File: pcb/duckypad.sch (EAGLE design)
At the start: 159 parts, among them IC2 REG1117, SW1 SPST_TACT-EVQQ2, SW2 SPST_TACT-EVQQ2, SW21 EC12E_SW, SW22 EC12E_SW, SW3 324_SW324_SWITCH_FOOT_HOLE, SW4 324_SW324_SWITCH_FOOT_HOLE, U1 USBC_16P, U2 USBC_16P, U3 ESP32-S3FN8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

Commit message: working on new PCB
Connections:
- removed net N$66: U3.SPICS1, X3-5.S
- net GND: now also X3-5.S
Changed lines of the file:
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@@
 <pinref part="X3" gate="-2" pin="S"/>
 <pinref part="GND64" gate="1" pin="GND"/>
-<wire x1="93.98" y1="-205.74" x2="83.82" y2="-205.74" width="0.1524" layer="91"/>
+<wire x1="93.98" y1="-205.74" x2="88.9" y2="-205.74" width="0.1524" layer="91"/>
+<pinref part="X3" gate="-5" pin="S"/>
+<wire x1="88.9" y1="-205.74" x2="83.82" y2="-205.74" width="0.1524" layer="91"/>
+<wire x1="93.98" y1="-213.36" x2="88.9" y2="-213.36" width="0.1524" layer="91"/>
+<wire x1="88.9" y1="-213.36" x2="88.9" y2="-205.74" width="0.1524" layer="91"/>
+<junction x="88.9" y="-205.74"/>
 </segment>
 <segment>
@@
 </segment>
 </net>
-<net name="N$66" class="0">
-<segment>
-<pinref part="U3" gate="G$1" pin="SPICS1"/>
-<wire x1="347.98" y1="-91.44" x2="365.76" y2="-91.44" width="0.1524" layer="91"/>
-<wire x1="365.76" y1="-91.44" x2="365.76" y2="-213.36" width="0.1524" layer="91"/>
-<wire x1="365.76" y1="-213.36" x2="93.98" y2="-213.36" width="0.1524" layer="91"/>
-<pinref part="X3" gate="-5" pin="S"/>
-</segment>
-</net>

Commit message: finishing touches
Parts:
- removed X3: SM12B-SSR-H-TB, duckypad:SM12B-SSR-H-TB
- added U$3: SH10P, duckypad:SH10P
- D1, D10, D11, D12, D13, D14, D15, D16, D17, D18, D19, D2, D20, D21, D3, D4, D5, D6, D7, D8, D9: device adafruit_changed:DIODESOD-123 -> duckypad:ADAFRUIT_CHANGED_DIODESOD-123
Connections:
- net +3V3: now also U$3.3; no longer X3-3.S
- net GND: now also U$3.11, U$3.12, U$3.2; no longer X3-12.S, X3-13.S, X3-14.S, X3-2.S, X3-5.S
- net N$1: now also U$3.1; no longer X3-1.S
- net N$37: now also U$3.4; no longer X3-4.S
- net N$67: now also U$3.5; no longer X3-6.S
- net N$68: now also U$3.6; no longer X3-7.S
- net N$69: now also U$3.7; no longer X3-8.S
- net N$70: now also U$3.8; no longer X3-9.S
- net N$72: now also U$3.9; no longer X3-10.S
- net N$73: now also U$3.10; no longer X3-11.S

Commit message: finishing touches
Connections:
- removed net N$32: C29.2, IC2.VIN, JP2.2
- new net N$66: C29.2, IC2.VIN, JP2.2, U$3.1, U1.VBUS
- net N$1: no longer U$3.1, U1.VBUS
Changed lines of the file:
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@@
 <segment>
 <pinref part="U2" gate="G$1" pin="VBUS"/>
-<wire x1="43.18" y1="-144.78" x2="78.74" y2="-144.78" width="0.1524" layer="91"/>
-<pinref part="U1" gate="G$1" pin="VBUS"/>
-<wire x1="43.18" y1="-177.8" x2="78.74" y2="-177.8" width="0.1524" layer="91"/>
-<wire x1="78.74" y1="-177.8" x2="78.74" y2="-144.78" width="0.1524" layer="91"/>
-<wire x1="78.74" y1="-144.78" x2="93.98" y2="-144.78" width="0.1524" layer="91"/>
-<junction x="78.74" y="-144.78"/>
+<wire x1="43.18" y1="-144.78" x2="93.98" y2="-144.78" width="0.1524" layer="91"/>
 <pinref part="JP2" gate="A" pin="1"/>
 <wire x1="93.98" y1="-144.78" x2="93.98" y2="-154.94" width="0.1524" layer="91"/>
-<junction x="78.74" y="-177.8"/>
-<pinref part="U$3" gate="G$1" pin="1"/>
-<wire x1="78.74" y1="-177.8" x2="124.46" y2="-177.8" width="0.1524" layer="91"/>
-<wire x1="124.46" y1="-177.8" x2="124.46" y2="-203.2" width="0.1524" layer="91"/>
 </segment>
 </net>
@@
 <pinref part="X1" gate="G$1" pin="SIGNAL"/>
 <wire x1="347.98" y1="-35.56" x2="281.94" y2="-35.56" width="0.1524" layer="91"/>
-</segment>
-</net>
-<net name="N$32" class="0">
-<segment>
-<pinref part="IC2" gate="G$1" pin="VIN"/>
-<pinref part="C29" gate="G$1" pin="2"/>
-<wire x1="119.38" y1="-144.78" x2="124.46" y2="-144.78" width="0.1524" layer="91"/>
-<wire x1="119.38" y1="-144.78" x2="96.52" y2="-144.78" width="0.1524" layer="91"/>
-<junction x="119.38" y="-144.78"/>
-<pinref part="JP2" gate="A" pin="2"/>
-<wire x1="96.52" y1="-144.78" x2="96.52" y2="-154.94" width="0.1524" layer="91"/>
 </segment>
 </net>
@@
 </segment>
 </net>
+<net name="N$66" class="0">
+<segment>
+<pinref part="U1" gate="G$1" pin="VBUS"/>
+<wire x1="43.18" y1="-177.8" x2="96.52" y2="-177.8" width="0.1524" layer="91"/>
+<pinref part="IC2" gate="G$1" pin="VIN"/>
+<pinref part="C29" gate="G$1" pin="2"/>
+<wire x1="119.38" y1="-144.78" x2="124.46" y2="-144.78" width="0.1524" layer="91"/>
+<wire x1="119.38" y1="-144.78" x2="96.52" y2="-144.78" width="0.1524" layer="91"/>
+<junction x="119.38" y="-144.78"/>
+<pinref part="JP2" gate="A" pin="2"/>
+<wire x1="96.52" y1="-144.78" x2="96.52" y2="-154.94" width="0.1524" layer="91"/>
+<pinref part="U$3" gate="G$1" pin="1"/>
+<wire x1="96.52" y1="-154.94" x2="96.52" y2="-177.8" width="0.1524" layer="91"/>
+<wire x1="96.52" y1="-177.8" x2="96.52" y2="-203.2" width="0.1524" layer="91"/>
+<wire x1="96.52" y1="-203.2" x2="124.46" y2="-203.2" width="0.1524" layer="91"/>
+<junction x="96.52" y="-154.94"/>
+<junction x="96.52" y="-177.8"/>
+</segment>
+</net>

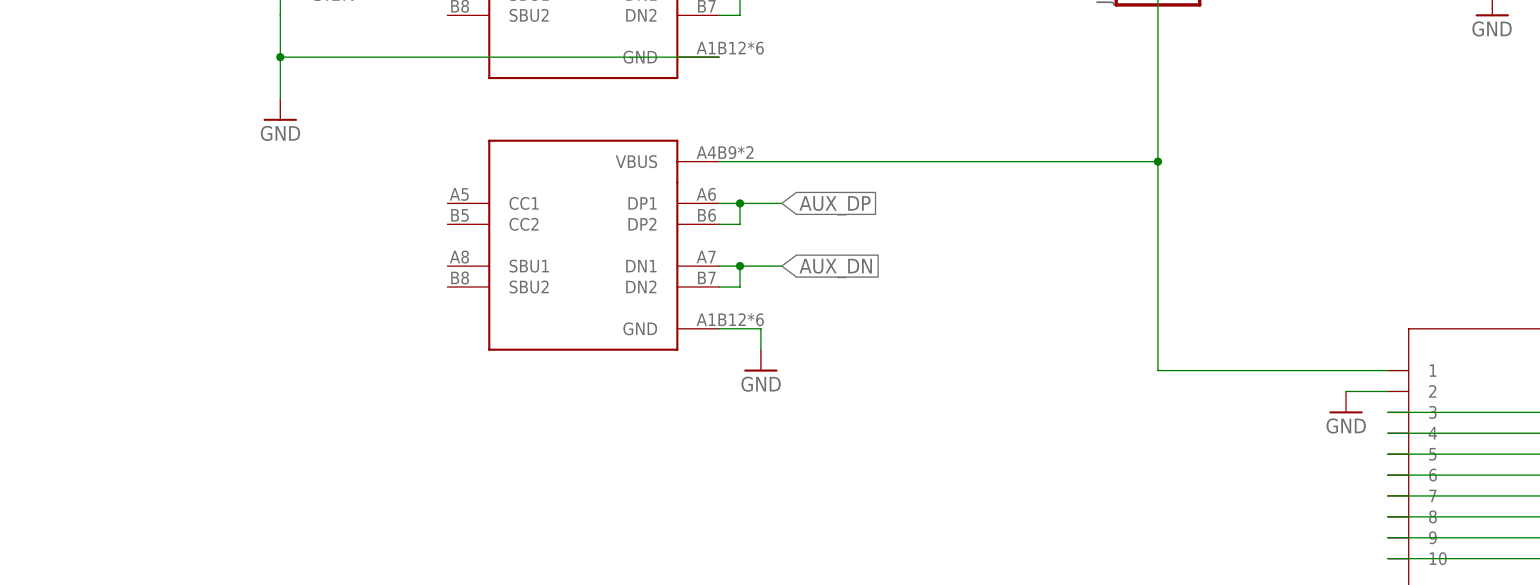
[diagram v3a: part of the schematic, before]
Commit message: wired up CC pins
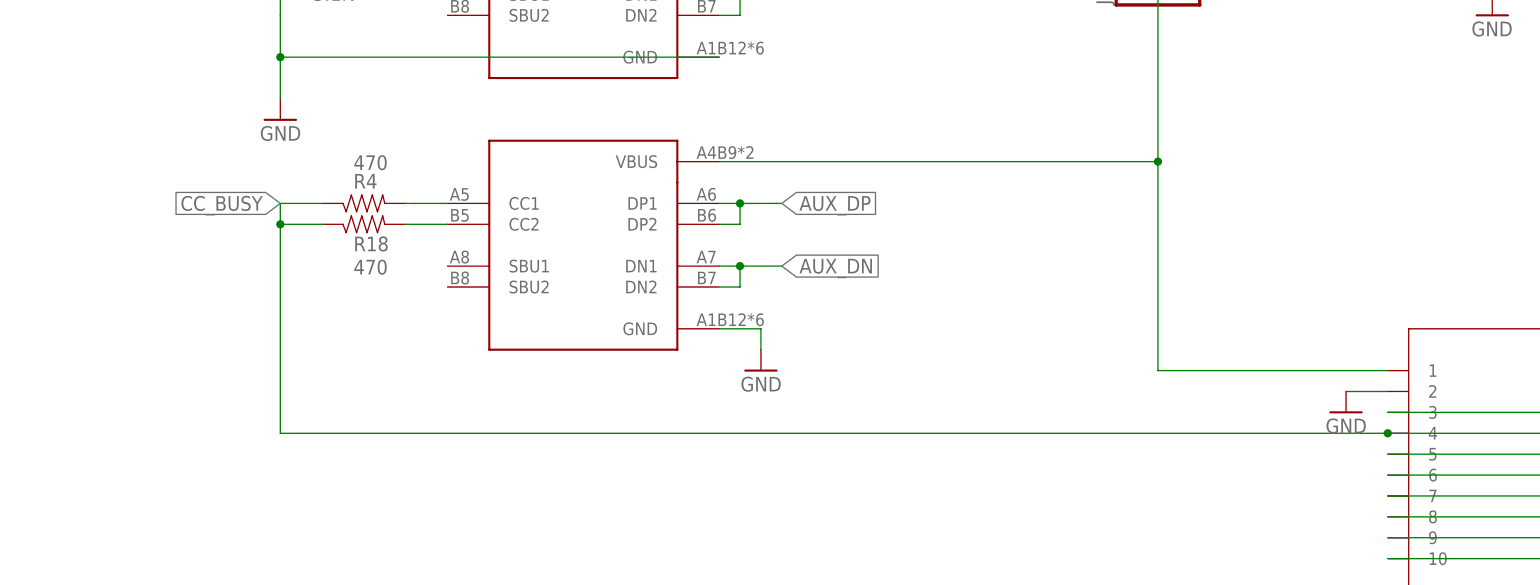
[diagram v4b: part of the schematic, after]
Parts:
- added R18, R4: 470, joyAnalog:RESISTOR0805-RES
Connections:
- removed net N$37: U$3.4, U3.GPIO21
- new net CC_BUSY: R18.1, R4.1, U$3.4, U3.GPIO21
- new net N$32: R4.2, U1.CC1
- new net N$80: R18.2, U1.CC2
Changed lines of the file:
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@@
 <part name="GND70" library="supply1" deviceset="GND" device=""/>
 <part name="GND64" library="supply1" deviceset="GND" device=""/>
+<part name="R4" library="joyAnalog" deviceset="RESISTOR" device="0805-RES" value="470"/>
+<part name="R18" library="joyAnalog" deviceset="RESISTOR" device="0805-RES" value="470"/>
 </parts>
 <sheets>
@@
 <instance part="GND64" gate="1" x="119.38" y="-236.22" smashed="yes" rot="MR0">
 <attribute name="VALUE" x="121.92" y="-238.76" size="1.778" layer="96" rot="MR0"/>
+</instance>
+<instance part="R4" gate="G$1" x="0" y="-182.88" smashed="yes" rot="MR180">
+<attribute name="NAME" x="-1.27" y="-179.2986" size="1.778" layer="95" rot="MR180"/>
+<attribute name="VALUE" x="-1.27" y="-177.038" size="1.778" layer="96" rot="MR180"/>
+</instance>
+<instance part="R18" gate="G$1" x="0" y="-185.42" smashed="yes" rot="MR180">
+<attribute name="NAME" x="-1.27" y="-186.9186" size="1.778" layer="95" rot="MR180"/>
+<attribute name="VALUE" x="-1.27" y="-189.738" size="1.778" layer="96" rot="MR180"/>
 </instance>
 </instances>
@@
 </segment>
 </net>
-<net name="N$37" class="0">
+<net name="CC_BUSY" class="0">
 <segment>
 <pinref part="U3" gate="G$1" pin="GPIO21"/>
@@
 <pinref part="U$3" gate="G$1" pin="4"/>
 <wire x1="124.46" y1="-210.82" x2="368.3" y2="-210.82" width="0.1524" layer="91"/>
+<pinref part="R4" gate="G$1" pin="1"/>
+<wire x1="-5.08" y1="-182.88" x2="-10.16" y2="-182.88" width="0.1524" layer="91"/>
+<pinref part="R18" gate="G$1" pin="1"/>
+<wire x1="-10.16" y1="-182.88" x2="-10.16" y2="-185.42" width="0.1524" layer="91"/>
+<wire x1="-10.16" y1="-185.42" x2="-5.08" y2="-185.42" width="0.1524" layer="91"/>
+<wire x1="124.46" y1="-210.82" x2="-10.16" y2="-210.82" width="0.1524" layer="91"/>
+<wire x1="-10.16" y1="-210.82" x2="-10.16" y2="-185.42" width="0.1524" layer="91"/>
+<junction x="124.46" y="-210.82"/>
+<junction x="-10.16" y="-185.42"/>
+<label x="-10.16" y="-182.88" size="1.778" layer="95" rot="R180" xref="yes"/>
 </segment>
 </net>
@@
 </segment>
 </net>
+<net name="N$32" class="0">
+<segment>
+<pinref part="R4" gate="G$1" pin="2"/>
+<pinref part="U1" gate="G$1" pin="CC1"/>
+<wire x1="5.08" y1="-182.88" x2="10.16" y2="-182.88" width="0.1524" layer="91"/>
+</segment>
+</net>
+<net name="N$80" class="0">
+<segment>
+<pinref part="R18" gate="G$1" pin="2"/>
+<pinref part="U1" gate="G$1" pin="CC2"/>
+<wire x1="5.08" y1="-185.42" x2="10.16" y2="-185.42" width="0.1524" layer="91"/>
+</segment>
+</net>

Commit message: adjusted component values
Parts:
- C1, C10, C2, C9: value 10nF -> 100nF
- C27: value 47uF -> 100uF
- C29: value 10uF -> 4.7uF
- C34, C38: value 2.2uF -> 4.7uF
- C35: value 22pF -> 12pF
- C4: value 1uF -> 100nF
- R13, R14, R15, R2, R8: value 10K -> 62K
- R5: value 5.1K -> 10K

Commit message: finishing touches
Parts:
- removed SJ1: (no value), jumper:SJ
- added R19: 999999, joyAnalog:RESISTOR0805-RES
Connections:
- net N$41: now also R19.1; no longer SJ1.2
- net RESET: now also R19.2; no longer SJ1.1
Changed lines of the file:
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@@
 <part name="D21" library="duckypad" deviceset="ADAFRUIT_CHANGED_DIODE" device="SOD-123"/>
 <part name="GND1" library="supply1" library_urn="urn:adsk.eagle:library:371" deviceset="GND" device=""/>
-<part name="SJ1" library="jumper" library_urn="urn:adsk.eagle:library:252" deviceset="SJ" device="" package3d_urn="urn:adsk.eagle:package:15471/1"/>
 <part name="GND54" library="clock" deviceset="GND" device=""/>
 <part name="GND61" library="supply1" library_urn="urn:adsk.eagle:library:371" deviceset="GND" device=""/>
@@
 <part name="R4" library="joyAnalog" deviceset="RESISTOR" device="0805-RES" value="470"/>
 <part name="R18" library="joyAnalog" deviceset="RESISTOR" device="0805-RES" value="470"/>
+<part name="R19" library="joyAnalog" deviceset="RESISTOR" device="0805-RES" value="999999"/>
 </parts>
 <sheets>
@@
 <attribute name="VALUE" x="327.66" y="-271.78" size="1.778" layer="96"/>
 </instance>
-<instance part="SJ1" gate="1" x="342.9" y="-5.08" smashed="yes" rot="R90">
-<attribute name="NAME" x="340.36" y="-7.62" size="1.778" layer="95" rot="R90"/>
-<attribute name="VALUE" x="346.71" y="-7.62" size="1.778" layer="96" rot="R90"/>
-</instance>
 <instance part="GND54" gate="1" x="419.1" y="10.16" smashed="yes">
 <attribute name="VALUE" x="416.56" y="7.62" size="1.778" layer="96"/>
@@
 <attribute name="NAME" x="-1.27" y="-186.9186" size="1.778" layer="95" rot="MR180"/>
 <attribute name="VALUE" x="-1.27" y="-189.738" size="1.778" layer="96" rot="MR180"/>
+</instance>
+<instance part="R19" gate="G$1" x="342.9" y="-5.08" smashed="yes" rot="MR270">
+<attribute name="NAME" x="341.4014" y="-1.27" size="1.778" layer="95" rot="MR270"/>
+<attribute name="VALUE" x="346.202" y="-1.27" size="1.778" layer="96" rot="MR270"/>
+<attribute name="NAME" x="341.4014" y="-1.27" size="1.778" layer="95" rot="MR270"/>
+<attribute name="VALUE" x="346.202" y="-1.27" size="1.778" layer="96" rot="MR270"/>
 </instance>
 </instances>
@@
 <wire x1="314.96" y1="-10.16" x2="325.12" y2="-10.16" width="0.1524" layer="91"/>
 <junction x="314.96" y="-10.16"/>
-<pinref part="SJ1" gate="1" pin="1"/>
+<pinref part="R19" gate="G$1" pin="2"/>
 <junction x="342.9" y="-10.16"/>
 </segment>
@@
 <wire x1="375.92" y1="-38.1" x2="375.92" y2="0" width="0.1524" layer="91"/>
 <junction x="398.78" y="-38.1"/>
-<pinref part="SJ1" gate="1" pin="2"/>
 <wire x1="375.92" y1="0" x2="342.9" y2="0" width="0.1524" layer="91"/>
-</segment>
-</net>
+<pinref part="R19" gate="G$1" pin="1"/>
+</segment>
+</net>

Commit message: finishing touches
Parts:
- D1, D10, D11, D12, D13, D14, D15, D16, D17, D18, D19, D2, D20, D21, D3, D4, D5, D6, D7, D8, D9: value (none) -> 1N4148
- L2: value PRS4018-4R7MT -> 4.7uH
- R19: value 999999 -> DNP
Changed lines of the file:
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@@
 <part name="R16" library="joyAnalog" deviceset="RESISTOR" device="0805-RES" value="10K"/>
 <part name="+3V35" library="supply1" library_urn="urn:adsk.eagle:library:371" deviceset="+3V3" device=""/>
-<part name="L2" library="Discrete" deviceset="L*" device="-4030" value="PRS4018-4R7MT"/>
+<part name="L2" library="Discrete" deviceset="L*" device="-4030" value="4.7uH"/>
 <part name="C46" library="clock" deviceset="CAP" device="0805" value="4.7uF"/>
 <part name="R17" library="joyAnalog" deviceset="RESISTOR" device="0805-RES" value="10K"/>
 <part name="GND62" library="supply1" library_urn="urn:adsk.eagle:library:371" deviceset="GND" device=""/>
 <part name="JP3" library="adafruit_changed" deviceset="PINHD-1X1" device="CB"/>
-<part name="D1" library="duckypad" deviceset="ADAFRUIT_CHANGED_DIODE" device="SOD-123"/>
+<part name="D1" library="duckypad" deviceset="ADAFRUIT_CHANGED_DIODE" device="SOD-123" value="1N4148"/>
 <part name="SW4" library="3pos_slide_switch" deviceset="324_SW" device="324_SWITCH_FOOT_HOLE" value="324_SW324_SWITCH_FOOT_HOLE"/>
-<part name="D2" library="duckypad" deviceset="ADAFRUIT_CHANGED_DIODE" device="SOD-123"/>
-<part name="D3" library="duckypad" deviceset="ADAFRUIT_CHANGED_DIODE" device="SOD-123"/>
-<part name="D4" library="duckypad" deviceset="ADAFRUIT_CHANGED_DIODE" device="SOD-123"/>
-<part name="D5" library="duckypad" deviceset="ADAFRUIT_CHANGED_DIODE" device="SOD-123"/>
-<part name="D6" library="duckypad" deviceset="ADAFRUIT_CHANGED_DIODE" device="SOD-123"/>
-<part name="D7" library="duckypad" deviceset="ADAFRUIT_CHANGED_DIODE" device="SOD-123"/>
-<part name="D8" library="duckypad" deviceset="ADAFRUIT_CHANGED_DIODE" device="SOD-123"/>
-<part name="D9" library="duckypad" deviceset="ADAFRUIT_CHANGED_DIODE" device="SOD-123"/>
-<part name="D10" library="duckypad" deviceset="ADAFRUIT_CHANGED_DIODE" device="SOD-123"/>
-<part name="D11" library="duckypad" deviceset="ADAFRUIT_CHANGED_DIODE" device="SOD-123"/>
-<part name="D12" library="duckypad" deviceset="ADAFRUIT_CHANGED_DIODE" device="SOD-123"/>
-<part name="D13" library="duckypad" deviceset="ADAFRUIT_CHANGED_DIODE" device="SOD-123"/>
-<part name="D14" library="duckypad" deviceset="ADAFRUIT_CHANGED_DIODE" device="SOD-123"/>
-<part name="D15" library="duckypad" deviceset="ADAFRUIT_CHANGED_DIODE" device="SOD-123"/>
-<part name="D16" library="duckypad" deviceset="ADAFRUIT_CHANGED_DIODE" device="SOD-123"/>
-<part name="D17" library="duckypad" deviceset="ADAFRUIT_CHANGED_DIODE" device="SOD-123"/>
-<part name="D18" library="duckypad" deviceset="ADAFRUIT_CHANGED_DIODE" device="SOD-123"/>
-<part name="D19" library="duckypad" deviceset="ADAFRUIT_CHANGED_DIODE" device="SOD-123"/>
-<part name="D20" library="duckypad" deviceset="ADAFRUIT_CHANGED_DIODE" device="SOD-123"/>
-<part name="D21" library="duckypad" deviceset="ADAFRUIT_CHANGED_DIODE" device="SOD-123"/>
+<part name="D2" library="duckypad" deviceset="ADAFRUIT_CHANGED_DIODE" device="SOD-123" value="1N4148"/>
+<part name="D3" library="duckypad" deviceset="ADAFRUIT_CHANGED_DIODE" device="SOD-123" value="1N4148"/>
+<part name="D4" library="duckypad" deviceset="ADAFRUIT_CHANGED_DIODE" device="SOD-123" value="1N4148"/>
+<part name="D5" library="duckypad" deviceset="ADAFRUIT_CHANGED_DIODE" device="SOD-123" value="1N4148"/>
+<part name="D6" library="duckypad" deviceset="ADAFRUIT_CHANGED_DIODE" device="SOD-123" value="1N4148"/>
+<part name="D7" library="duckypad" deviceset="ADAFRUIT_CHANGED_DIODE" device="SOD-123" value="1N4148"/>
+<part name="D8" library="duckypad" deviceset="ADAFRUIT_CHANGED_DIODE" device="SOD-123" value="1N4148"/>
+<part name="D9" library="duckypad" deviceset="ADAFRUIT_CHANGED_DIODE" device="SOD-123" value="1N4148"/>
+<part name="D10" library="duckypad" deviceset="ADAFRUIT_CHANGED_DIODE" device="SOD-123" value="1N4148"/>
+<part name="D11" library="duckypad" deviceset="ADAFRUIT_CHANGED_DIODE" device="SOD-123" value="1N4148"/>
+<part name="D12" library="duckypad" deviceset="ADAFRUIT_CHANGED_DIODE" device="SOD-123" value="1N4148"/>
+<part name="D13" library="duckypad" deviceset="ADAFRUIT_CHANGED_DIODE" device="SOD-123" value="1N4148"/>
+<part name="D14" library="duckypad" deviceset="ADAFRUIT_CHANGED_DIODE" device="SOD-123" value="1N4148"/>
+<part name="D15" library="duckypad" deviceset="ADAFRUIT_CHANGED_DIODE" device="SOD-123" value="1N4148"/>
+<part name="D16" library="duckypad" deviceset="ADAFRUIT_CHANGED_DIODE" device="SOD-123" value="1N4148"/>
+<part name="D17" library="duckypad" deviceset="ADAFRUIT_CHANGED_DIODE" device="SOD-123" value="1N4148"/>
+<part name="D18" library="duckypad" deviceset="ADAFRUIT_CHANGED_DIODE" device="SOD-123" value="1N4148"/>
+<part name="D19" library="duckypad" deviceset="ADAFRUIT_CHANGED_DIODE" device="SOD-123" value="1N4148"/>
+<part name="D20" library="duckypad" deviceset="ADAFRUIT_CHANGED_DIODE" device="SOD-123" value="1N4148"/>
+<part name="D21" library="duckypad" deviceset="ADAFRUIT_CHANGED_DIODE" device="SOD-123" value="1N4148"/>
 <part name="GND1" library="supply1" library_urn="urn:adsk.eagle:library:371" deviceset="GND" device=""/>
 <part name="GND54" library="clock" deviceset="GND" device=""/>
@@
 <part name="R4" library="joyAnalog" deviceset="RESISTOR" device="0805-RES" value="470"/>
 <part name="R18" library="joyAnalog" deviceset="RESISTOR" device="0805-RES" value="470"/>
-<part name="R19" library="joyAnalog" deviceset="RESISTOR" device="0805-RES" value="999999"/>
+<part name="R19" library="joyAnalog" deviceset="RESISTOR" device="0805-RES" value="DNP"/>
 </parts>
 <sheets>
@@
 <instance part="L2" gate="L" x="190.5" y="-252.73" smashed="yes">
 <attribute name="NAME" x="185.42" y="-251.46" size="1.27" layer="95"/>
-<attribute name="VALUE" x="182.88" y="-256.54" size="1.27" layer="96"/>
+<attribute name="VALUE" x="187.96" y="-256.54" size="1.27" layer="96"/>
 </instance>
 <instance part="C46" gate="G$1" x="233.68" y="-281.94" smashed="yes" rot="R180">
